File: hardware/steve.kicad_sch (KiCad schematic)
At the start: 32 parts

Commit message: Finished routing traces
Finished routing traces. Also added extra ground vias to stitch the ground planes together. Lessons for next time: power pads (on a microcontroller or other) should immediately get a via; passives can go on the back (including decoupling caps if power vias are close); everything should be spaced further; try not to put 2 unrelated components on top of each other; uC signal traces should be fanned out (mostly inwards) and via'd for ease of use
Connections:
- net +5V: no longer 5V-DiodeArr1.2 (K)
- net +5V_BATT: no longer 5V-DiodeArr1.1 (A)
- net +5V_USB: no longer 5V-DiodeArr1.3 (A)
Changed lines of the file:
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@@
 		(lib_id "Device:D_Schottky_Dual_CommonCathode_AKA_Parallel")
 		(at 194.31 88.9 0)
+		(mirror y)
 		(unit 1)
 		(exclude_from_sim no)
@@
 		(dnp no)
 		(property "Reference" "5V-DiodeArr1"
-			(at 204.47 91.186 0)
+			(at 184.15 91.186 0)
 			(effects
 				(font
@@
 		)
 		(property "Value" "Schottky Diode Array, 5A per, 40V"
-			(at 193.04 94.996 0)
+			(at 195.58 94.996 0)
 			(effects
 				(font
@@
 		)
 		(property "Footprint" "Imported_Footprints:PDS1040CTL-13_PowerDI-5"
-			(at 195.58 88.9 0)
+			(at 193.04 88.9 0)
 			(effects
 				(font
@@
 		)
 		(property "Datasheet" "https://www.digikey.com/en/products/detail/diodes-incorporated/PDS1040CTL-13/717933"
-			(at 195.58 88.9 0)
+			(at 193.04 88.9 0)
 			(effects
 				(font

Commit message: Schematic and Board fixes for Mfg
Schematic and Board fixes for Manufacturing. Added LCSC/JLC part numbers to values in schematic for BOM processing. Updated schematic fields. Added GND to each PSM connector. Brought PSM connector fix to PCB. Updated PCB designator locations from schematic changes.
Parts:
- 32K-Y2: renamed from 32.768kHz-Y2; value 32.768kHz -> 32.768kHz Crystal 12.5pf C90944
- 8M-Y1: renamed from 8MHz-Y1; value 8MHz -> 8MHz Crystal 10pf C400090
- BT0, RST1: value KMR221G -> Button KMR221G C72443
- D1: renamed from 5V-DiodeArr1; value Schottky Diode Array, 5A per, 40V -> 10A/5A Schottky Diode Arr C780876
- Flash1: value W25Q128JVSIQ -> W25Q128JVSIQ 128Mb SPI Flash C97521
- LDO-1: renamed from 3.3V-LinReg1; value TLV1117LV33DCYR -> 3.3V 1A Lin Reg C15578
- STM32F407-uC1: renamed from STM32F407-µC1; value STM32F407VGTx -> STM32F407VGTx Microcontroller C12345
- USBC-1: value USB_C_Receptacle_16P -> USB-C Receptacle 16P C3025063
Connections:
- net +5V: now also D1.2 (K)
- net +5V_BATT: now also D1.1 (A)
- net +5V_USB: now also D1.3 (A)
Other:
- moved on the sheet: BT0, C7, R1, R2

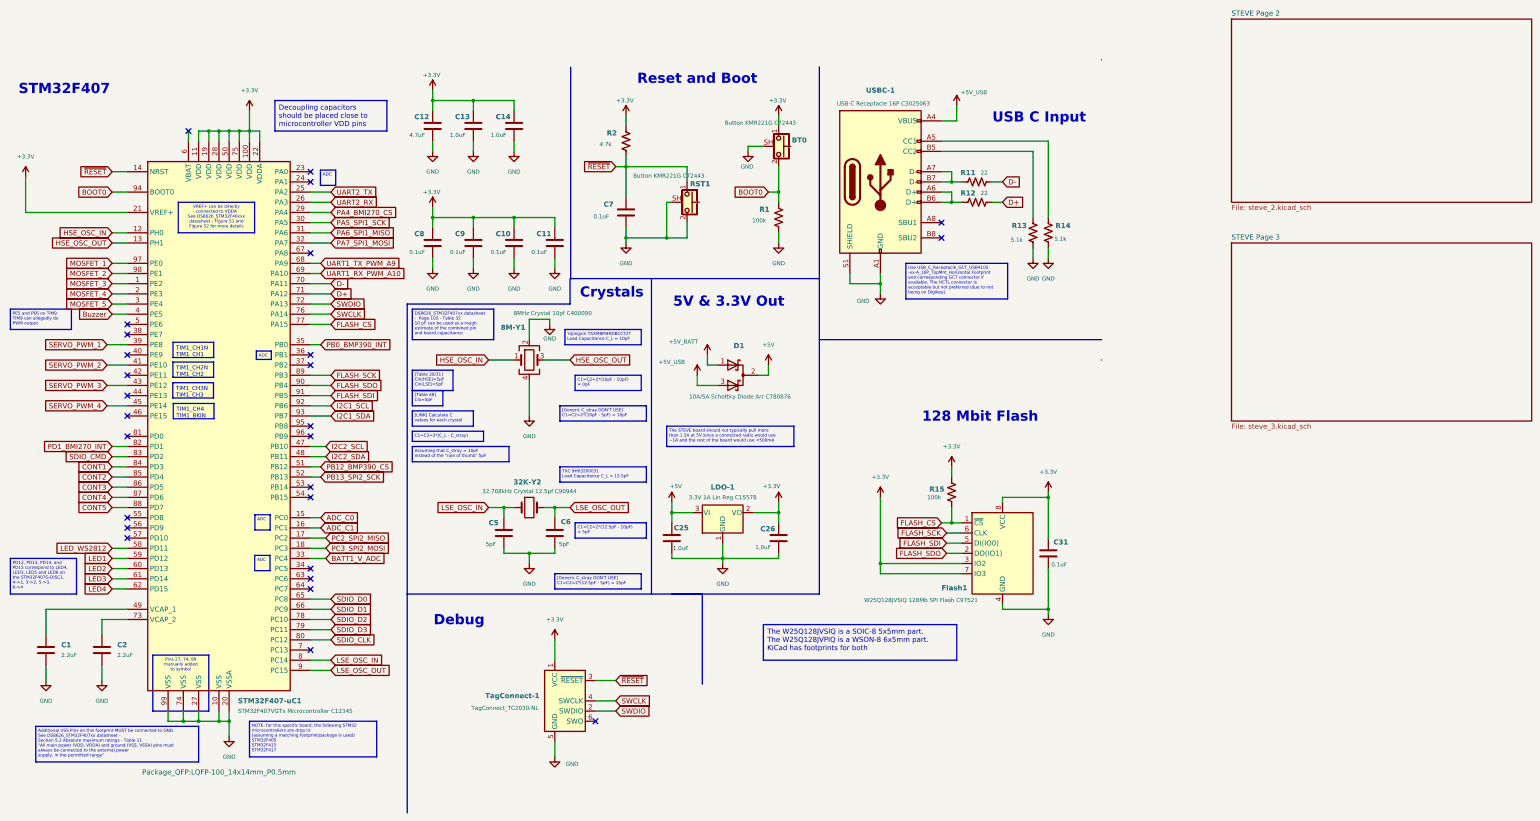
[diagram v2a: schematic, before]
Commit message: Fixed all ERC issues; fixed important DRC issues
Fixed all ERC Errors and Warnings in the schematic. Fixed all Errors and Warnings in the DRC for the board (Not counting JLC 4-Wire Kelvin test and plane thermal relief spoke errors that were manually reviewed and excluded).
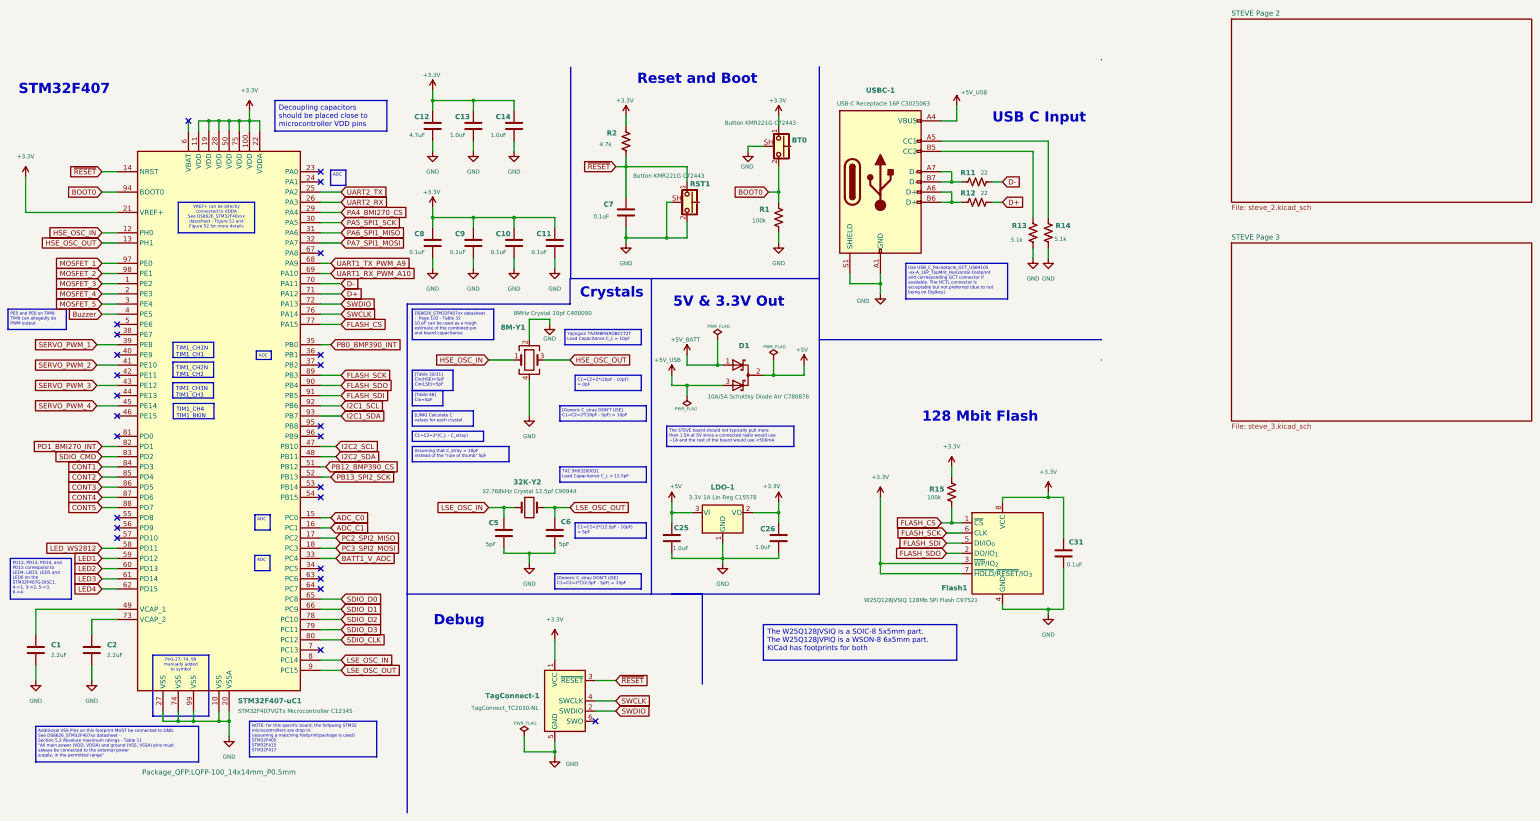
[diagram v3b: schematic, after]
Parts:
- Flash1: symbol Memory_Flash:W25Q128JVS -> Imported_Symbols:W25Q128JVS_PinsFixed
- STM32F407-uC1: symbol MCU_ST_STM32F4:STM32F407VGTx -> Imported_Symbols:STM32F407VGTx_All_GNDs
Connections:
- no-connect marks 27 -> 25
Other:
- moved on the sheet: C1, C2, C31, D1, Flash1, STM32F407-uC1
